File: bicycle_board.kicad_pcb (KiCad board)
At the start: 2 copper layers, 41.4 x 84.9 mm, 121 parts, among them J1 Micro_SD_Card, J10 USB_A, J11 Conn_01x04, J13 Conn_01x04, J2 USB_C_Receptacle_USB2.0_16P, J3 Conn_01x02, J4 Conn_01x02, J5 Conn_01x08, J6 Conn_01x04, J7 Conn_01x05, J8 Conn_01x02, J9 Conn_01x06, Q1 Q_NMOS_GSD, Q4 Q_NMOS_GSD, Q6 Si2302, Q7 Si2302, Q8 Q_PMOS_GSD, Q9 Q_PMOS_GSD, U1 TP4056, U11 BMP280, U12 MMC5633NJL, U13 NS4168, U14 ESP32-C3-WROOM-02U, U15 CH32V203C8T6, U16 PS7516, U17 TXB0108PW, U2 SGM2039, U3 IIM-42652, U4 QMI8610, U5 AHT20, U6 SGM2033-1.8, U7 74HC595, U8 SGM8040-1, U9 PCA9306DC1, Y1 12MHz, Y2 32.768kHz

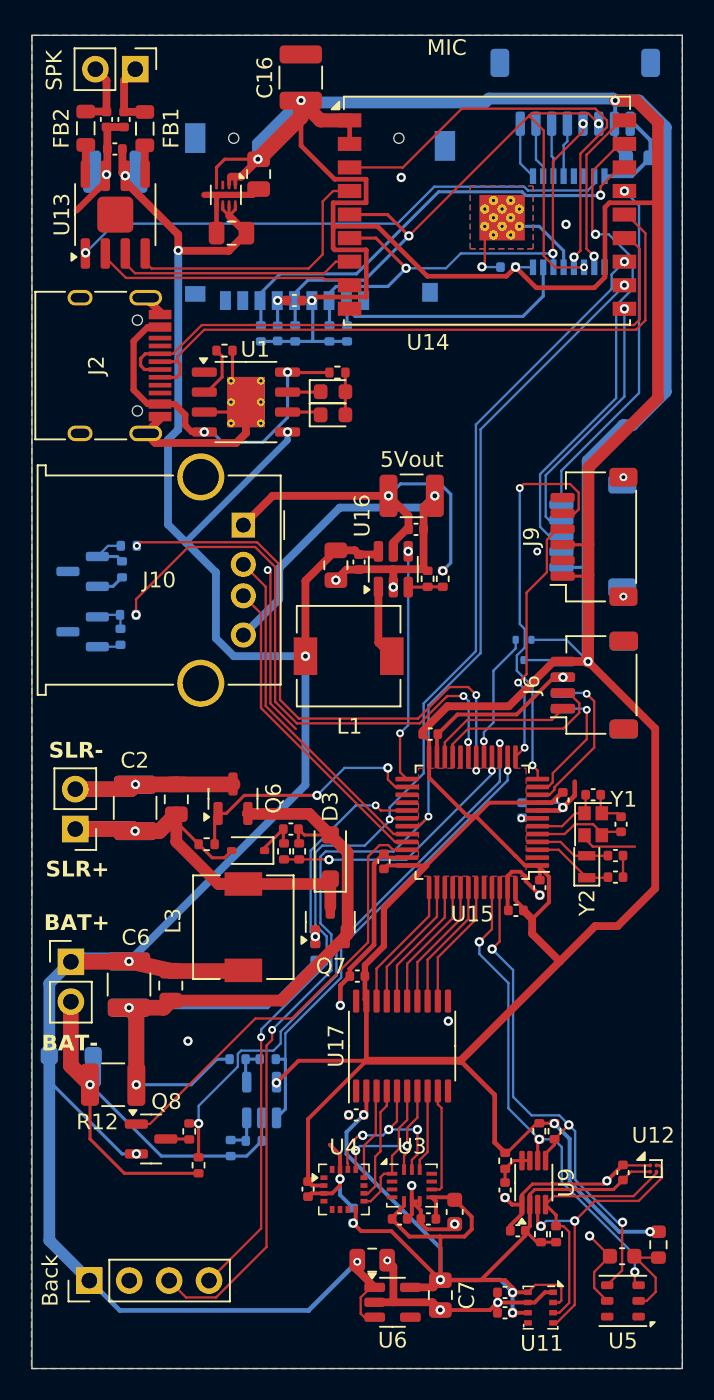
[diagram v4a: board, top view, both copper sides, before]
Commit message: 调整电源线宽度，一些走线布局
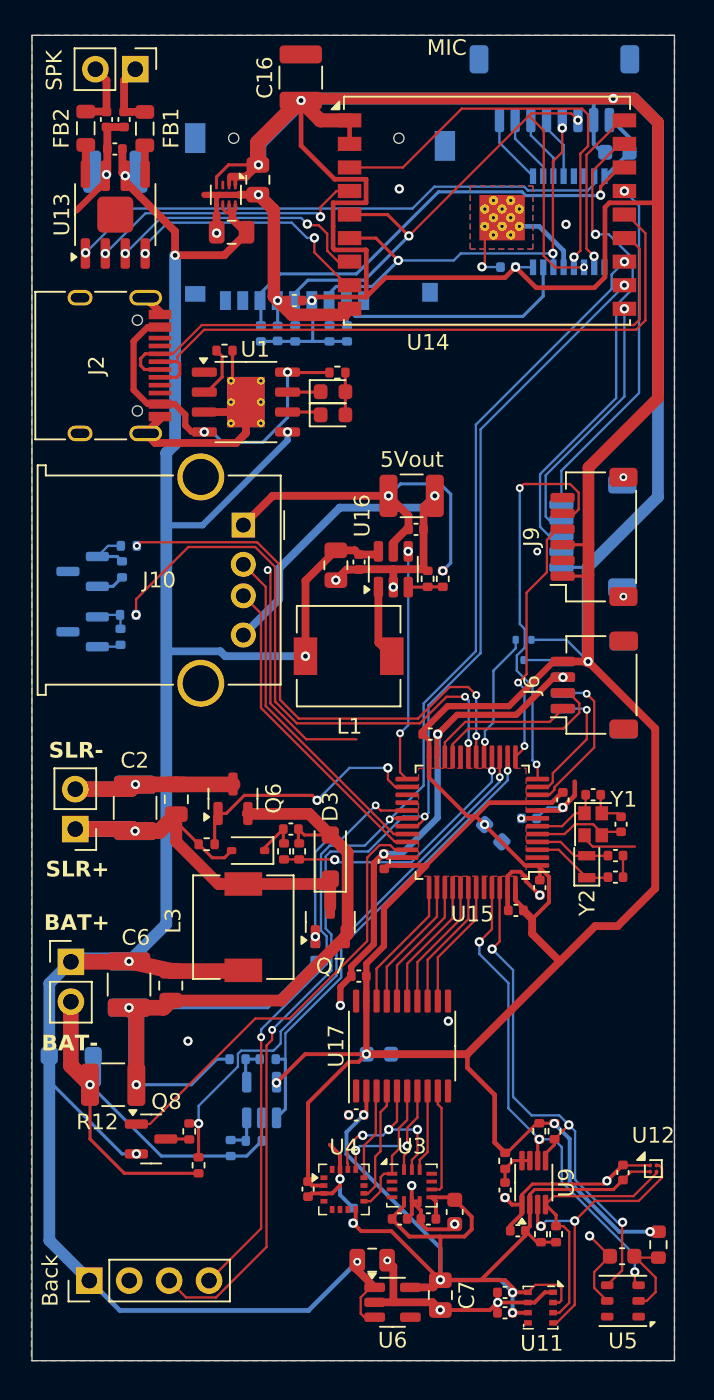
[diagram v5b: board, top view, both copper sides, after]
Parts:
- added C43: 2.2u, Capacitor_SMD:C_0603_1608Metric, B.Cu at (122.7, 122.0)
- added C49: 2.2u, Capacitor_SMD:C_0603_1608Metric, B.Cu at (130.0, 107.9)
- moved C14 1.37 mm to (137.9, 64.5)
- moved J5 1.34 mm to (133.9, 60.5)
- moved C48 0.68 mm to (132.2, 107.0), turned to 180 degrees
- moved C8 0.36 mm to (115.0, 66.3)
- moved C21 0.09 mm to (121.4, 117.0)
- moved C3 0.06 mm to (113.3, 69.6)
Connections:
- U14 pad 4: /I2SO_SD -> /I2SO_WS
- U14 pad 8: /I2SO_WS -> /I2SO_SD
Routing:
- net GND: track 212.0 -> 236.3 mm, vias 29 -> 33
- net +3.3V: track 339.0 -> 355.8 mm, vias 9 -> 11
- net /ADC_Vbat: track 37.0 -> 35.3 mm
- net /CH1: track 38.1 -> 36.4 mm
- net /I2SO_BCK: track 15.5 -> 17.0 mm, vias 0 -> 2
- net /SPI_MOSI: track 31.7 -> 30.2 mm
- net /595_RCLK: track 28.5 -> 27.0 mm
- net /I2SO_SD: track 17.8 -> 16.3 mm, vias 0 -> 2
- net /SPI_SCLK: track 42.9 -> 41.5 mm
- net /I2SO_WS: track 16.5 -> 17.8 mm, vias 0 -> 2
- net /CH2: track 36.7 -> 37.6 mm
- net /TXD: track 79.4 -> 78.6 mm
- net /SPI_CS_LCD: track 3.53 -> 4.31 mm
- net /LCD_BL: track 3.68 -> 4.46 mm
- net /LCD_RST: track 3.39 -> 4.17 mm
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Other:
- board size 41.4 x 84.9 mm -> 40.9 x 84.4 mm

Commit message: 接口添加TVS二极管和去耦电容，调整已有电容连接走线宽度
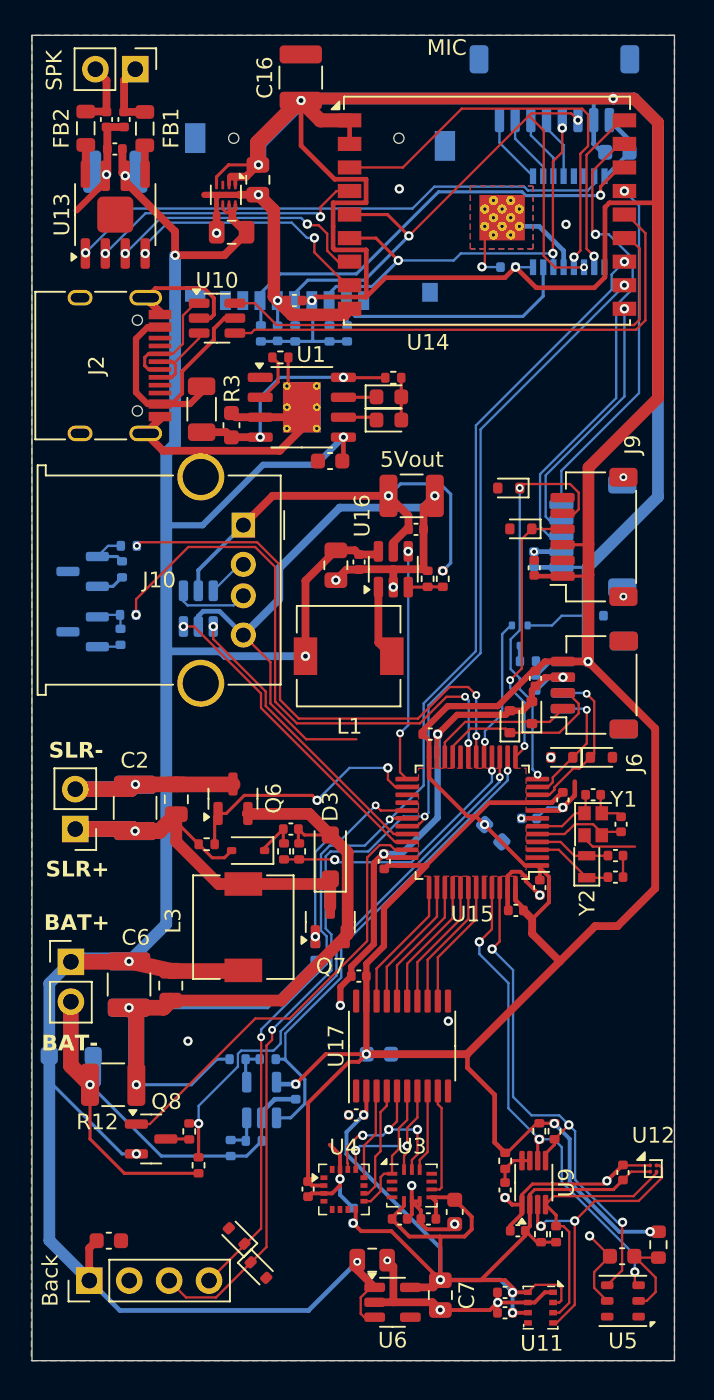
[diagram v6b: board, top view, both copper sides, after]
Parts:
- added C50: 1uf, Capacitor_SMD:C_0603_1608Metric, F.Cu at (113.3, 81.9)
- added C51: 0.1u, Capacitor_SMD:C_0402_1005Metric, B.Cu at (136.5, 94.1)
- added C52: 10nf, Capacitor_SMD:C_0402_1005Metric, B.Cu at (132.7, 98.3)
- added C53: 2.2u, Capacitor_SMD:C_0603_1608Metric, F.Cu at (105.5, 133.9)
- added C54: 0.1u, Capacitor_SMD:C_0402_1005Metric, F.Cu at (132.7, 98.0)
- added C55: 0.1u, Capacitor_SMD:C_0402_1005Metric, B.Cu at (132.6, 90.5)
- added C56: 0.1u, Capacitor_SMD:C_0402_1005Metric, F.Cu at (132.6, 91.0)
- added C57: 1uf, Capacitor_SMD:C_0603_1608Metric, F.Cu at (119.6, 84.2)
- added C58: 0.1u, Capacitor_SMD:C_0402_1005Metric, B.Cu at (117.4, 124.4)
- added D1: ESD5Zxx, Diode_SMD:D_SOD-523, F.Cu at (113.6, 133.6)
- added D10: ESD5Zxx, Diode_SMD:D_SOD-523, F.Cu at (132.4, 100.2)
- added D11: ESD5Zxx, Diode_SMD:D_SOD-523, F.Cu at (131.7, 88.5)
- added D12: ESD5Zxx, Diode_SMD:D_SOD-523, F.Cu at (115.0, 135.7)
- added D13: ESD5Zxx, Diode_SMD:D_SOD-523, F.Cu at (136.8, 103.1)
- added D2: ESD5Zxx, Diode_SMD:D_SOD-523, F.Cu at (131.0, 100.8)
- added D8: ESD5Zxx, Diode_SMD:D_SOD-523, F.Cu at (130.9, 85.9)
- added D9: ESD5Zxx, Diode_SMD:D_SOD-523, F.Cu at (134.3, 103.1)
- added R3: 0.4, Resistor_SMD:R_1206_3216Metric, F.Cu at (111.4, 80.9)
- added R4: 4.7, Resistor_SMD:R_0402_1005Metric, B.Cu at (132.2, 97.0)
- added U10: USBLC6-2SC6, Package_TO_SOT_SMD:SOT-23-6, F.Cu at (112.4, 75.1)
- added U18: USBLC6-2SC6, Package_TO_SOT_SMD:SOT-23-6, B.Cu at (111.2, 93.6)
- moved R13 3.59 mm to (116.4, 77.6)
- moved D5 3.57 mm to (123.3, 81.6)
- moved D6 3.57 mm to (123.3, 80.1)
- moved R22 3.57 mm to (123.6, 78.9)
- moved U1 3.57 mm to (117.8, 80.8)
- moved Q9 0.95 mm to (131.7, 95.3)
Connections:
- J10 pad 2: /USB_CH32FS_D- -> Net-(J10-D-)
- J10 pad 3: /USB_CH32FS_D+ -> Net-(J10-D+)
- J2 pad A6: /USB_ESP_D+ -> Net-(J2-D+-PadA6)
- J2 pad A7: /USB_ESP_D- -> Net-(J2-D--PadA7)
- J2 pad B6: /USB_ESP_D+ -> Net-(J2-D+-PadA6)
- J2 pad B7: /USB_ESP_D- -> Net-(J2-D--PadA7)
- Q9 pad 3: Net-(J11-Pin_1) -> Net-(Q9-D)
- R22 pad 1: /power/VUSB -> Net-(U1-CE)
- U1 pad 4: /power/VUSB -> Net-(U1-CE)
- U1 pad 8: /power/VUSB -> Net-(U1-CE)
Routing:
- net GND: track 236.3 -> 256.7 mm
- net Net-(U1-CE): track 0.00 -> 14.9 mm, vias 0 -> 2
- net /USB_ESP_D-: track 40.4 -> 32.3 mm
- net /USB_ESP_D+: track 41.8 -> 33.9 mm
- net Net-(J2-D--PadA7): track 0.00 -> 7.55 mm
- net +BATT: track 164.4 -> 171.8 mm
- net +5V: track 24.2 -> 29.6 mm
- net Net-(J2-D+-PadA6): track 0.00 -> 5.33 mm
- net Net-(J10-D+): track 0.00 -> 4.84 mm
- net /power/VUSB: track 23.0 -> 18.7 mm, vias 2 -> 0
- net +3.3V: track 355.8 -> 359.4 mm
- net /USB_CH32FS_D-: track 22.0 -> 18.8 mm, vias 0 -> 1
- net Net-(J10-D-): track 0.00 -> 2.61 mm
- net /ADC_Isolar: track 29.7 -> 31.3 mm
- net /ZW101_TX: track 16.3 -> 17.7 mm
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
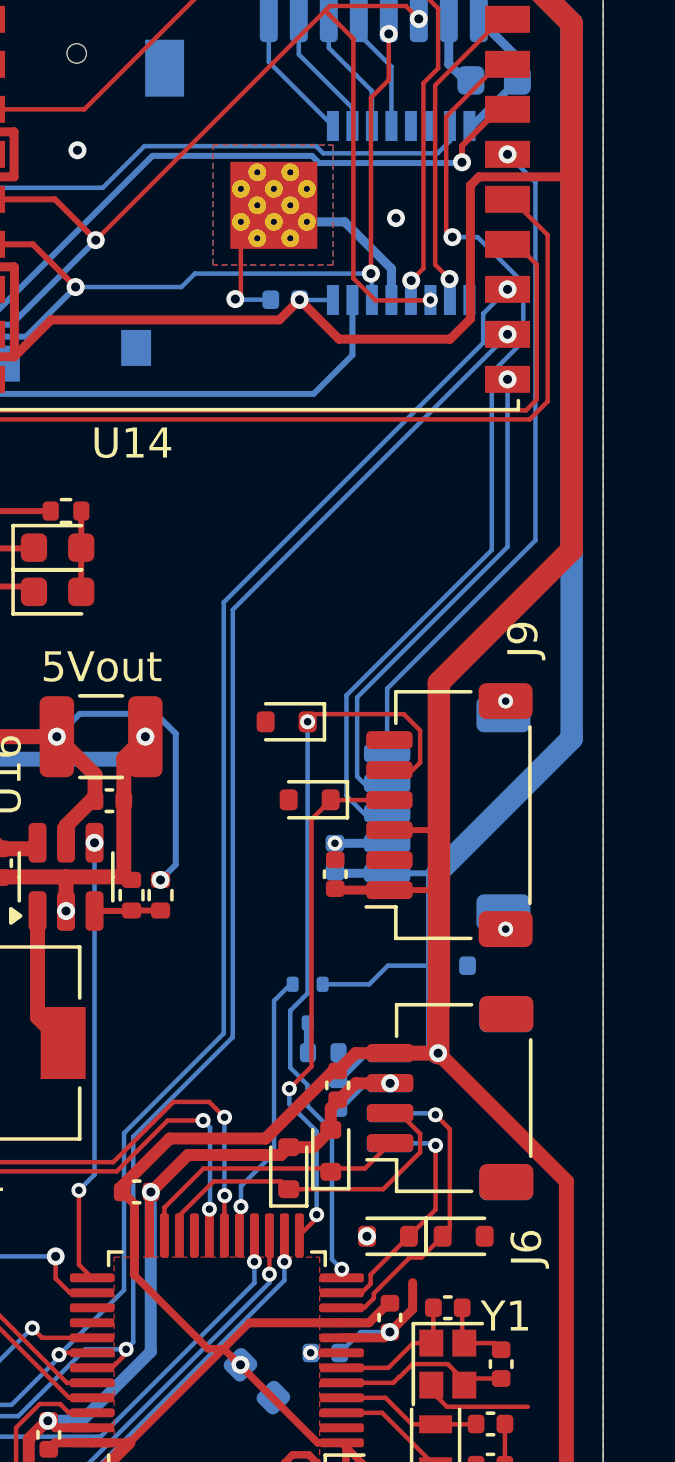
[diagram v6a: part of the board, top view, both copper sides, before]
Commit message: I2S麦克风接口添加TVS管
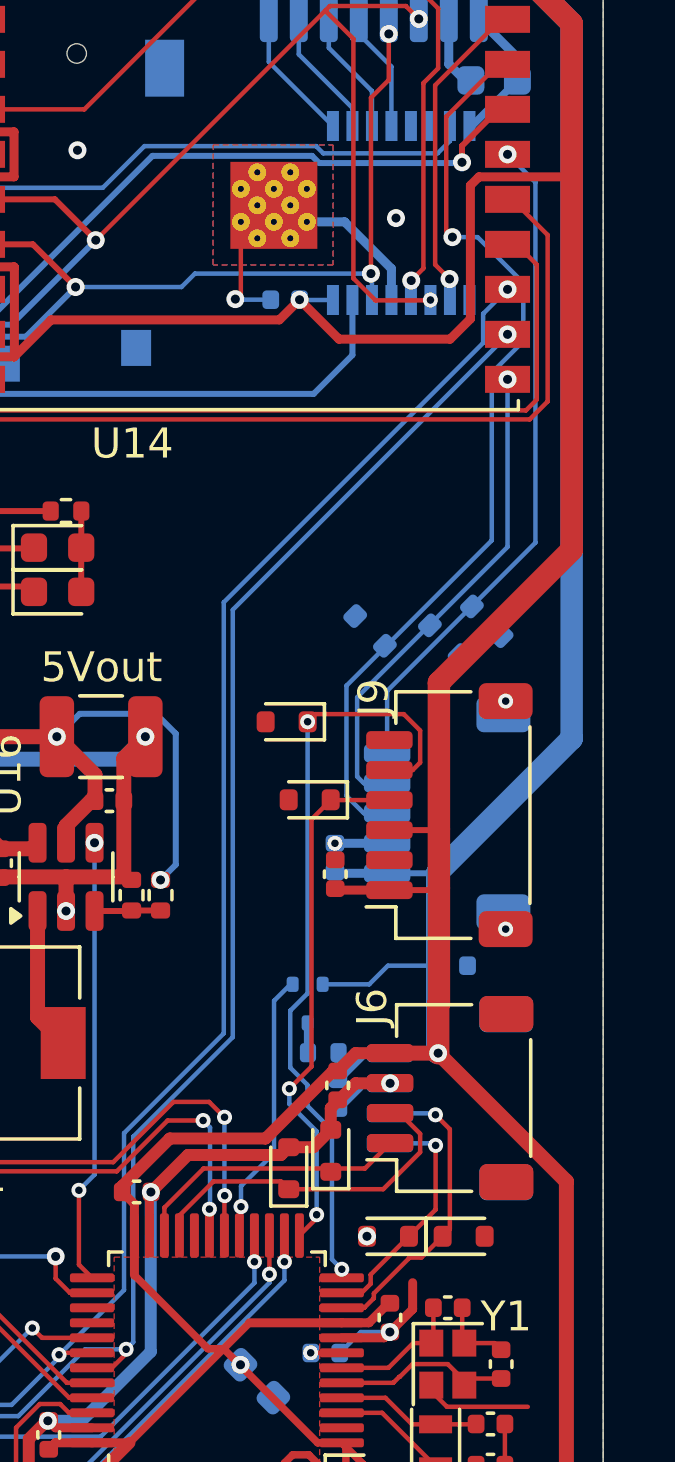
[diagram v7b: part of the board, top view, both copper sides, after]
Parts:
- added D14: ESD5Zxx, Diode_SMD:D_SOD-523, B.Cu at (137.6, 82.6)
- added D15: ESD5Zxx, Diode_SMD:D_SOD-523, B.Cu at (136.2, 83.2)
- added D16: ESD5Zxx, Diode_SMD:D_SOD-523, B.Cu at (133.7, 82.9)
